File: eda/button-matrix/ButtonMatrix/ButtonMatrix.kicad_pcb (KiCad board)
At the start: 2 copper layers, 87.2 x 87.2 mm, 54 parts, among them J1 Conn_01x12, J2 Conn_01x12, SW1 SW_Omron_B3FS, SW10 SW_Omron_B3FS, SW11 SW_Omron_B3FS, SW12 SW_Omron_B3FS, SW13 SW_Omron_B3FS, SW14 SW_Omron_B3FS, SW15 SW_Omron_B3FS, SW16 SW_Omron_B3FS, SW2 SW_Omron_B3FS, SW3 SW_Omron_B3FS, SW4 SW_Omron_B3FS, SW5 SW_Omron_B3FS, SW6 SW_Omron_B3FS, SW7 SW_Omron_B3FS, SW8 SW_Omron_B3FS, SW9 SW_Omron_B3FS

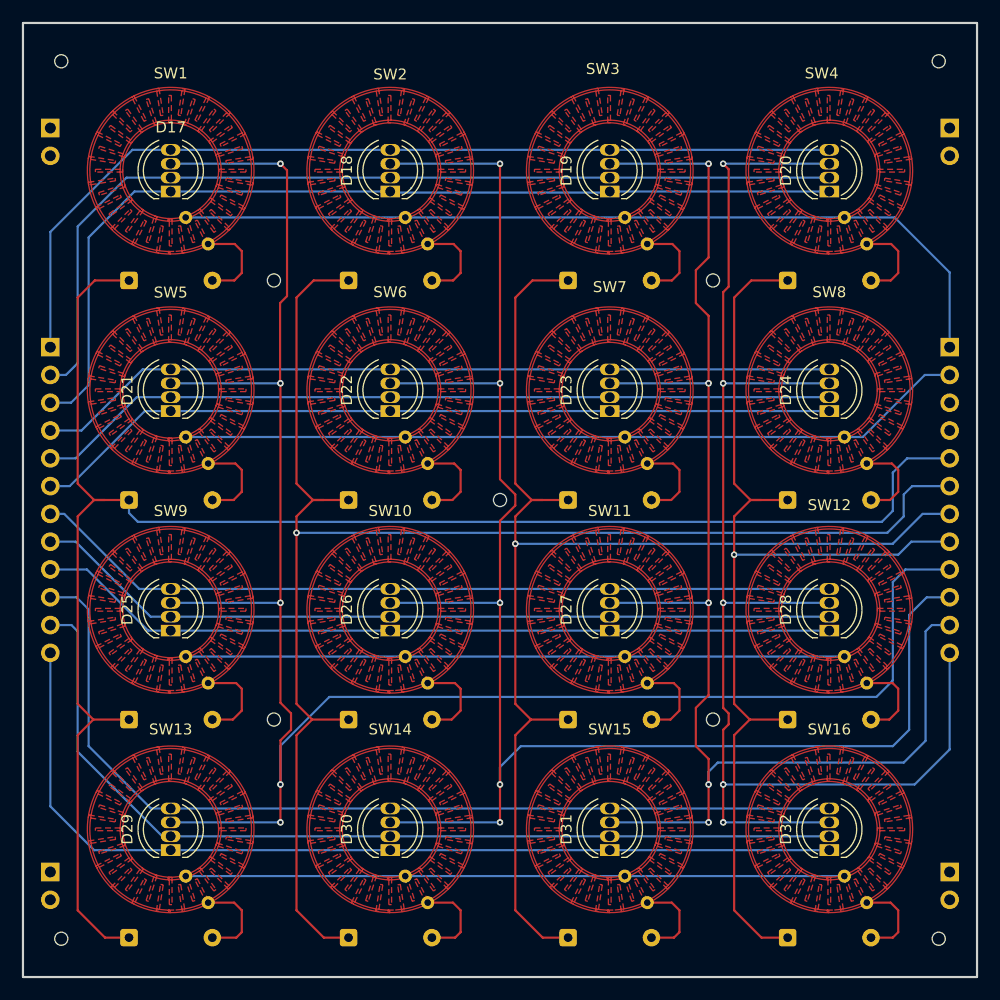
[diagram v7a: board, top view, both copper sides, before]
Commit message: - Fixed issue in my lumisquare button footrprint - Redesign teh button fill areas to better alingn witht he button mask
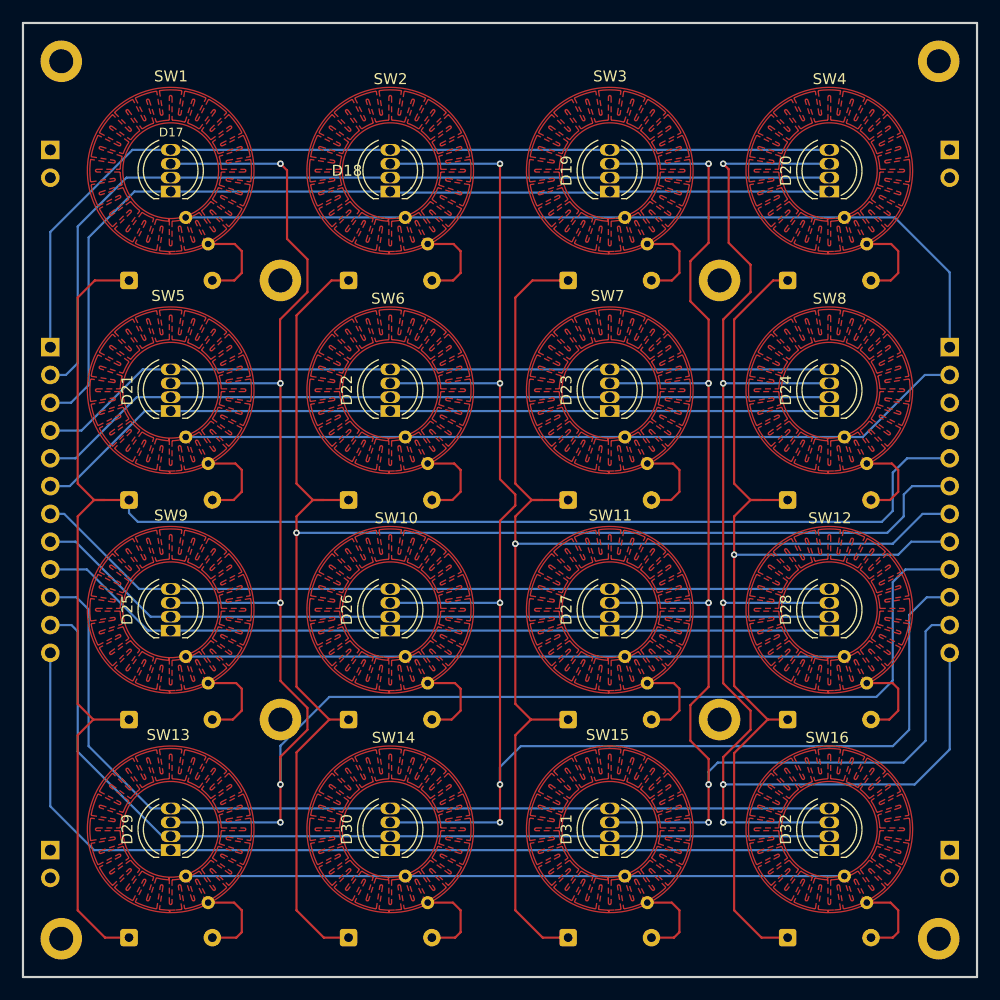
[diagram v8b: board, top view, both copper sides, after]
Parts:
- added REF**: M2, MountingHole:MountingHole_2.2mm_M2_DIN965_Pad, F.Cu at (191.7, 123.1)
- added REF**: M2, MountingHole:MountingHole_2.2mm_M2_DIN965_Pad, F.Cu at (131.5, 62.9)
- added REF**: M2, MountingHole:MountingHole_2.2mm_M2_DIN965_Pad, F.Cu at (211.7, 62.9)
- added REF**: M2, MountingHole:MountingHole_2.2mm_M2_DIN965_Pad, F.Cu at (191.7, 82.9)
- added REF**: M2, MountingHole:MountingHole_2.2mm_M2_DIN965_Pad, F.Cu at (131.5, 143.1)
- added REF**: M2, MountingHole:MountingHole_2.2mm_M2_DIN965_Pad, F.Cu at (151.5, 123.1)
- added REF**: M2, MountingHole:MountingHole_2.2mm_M2_DIN965_Pad, F.Cu at (151.5, 82.9)
- added REF**: M2, MountingHole:MountingHole_2.2mm_M2_DIN965_Pad, F.Cu at (211.7, 143.1)
- SW1, SW10, SW11, SW12, SW13, SW14, SW15, SW16, SW2, SW3, SW4, SW5, SW6, SW7, SW8, SW9: value SW_Omron_B3FS -> ~
- moved REF** 2.00 mm to (212.7, 71.0)
- moved REF** 2.00 mm to (212.7, 135.0)
- moved REF** 2.00 mm to (130.5, 71.0)
- moved REF** 2.00 mm to (130.5, 135.0)
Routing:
- net /LED_COL4: track 130.7 -> 134.0 mm
- net /LED_COL1: track 178.4 -> 181.1 mm
- net /SW_COL4: track 97.9 -> 96.5 mm
- net /SW_COL2: track 139.8 -> 138.6 mm
- net /LED_COL3: track 132.9 -> 133.7 mm
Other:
- outline, holes or cut-outs redrawn
